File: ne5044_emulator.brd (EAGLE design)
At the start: 17 x 23 mm, 13 parts, among them IC2 STM8S003F3, U1 NE5044_MINIMAL_PADS, U2 SPX1117M3-L-5-0

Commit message: - Daily save
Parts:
- moved SWIM 0.51 mm to (2.29, 6.35)
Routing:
- net GND: track 74.9 -> 75.9 mm, vias 4 -> 3
- net BTN0: track 35.4 -> 34.5 mm
- net BTN1: track 15.2 -> 14.3 mm
- net ADC_CH0: track 9.11 -> 9.95 mm
- net +5V: track 34.5 -> 33.7 mm
- net BTN2: track 16.0 -> 15.3 mm
- net ADC_CH2: track 10.5 -> 9.90 mm
- net BTN3: track 16.9 -> 16.3 mm
- net !STM8_RESET: track 14.1 -> 13.6 mm
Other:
- board size 17 x 23 mm -> 16.5 x 23 mm
- board text added: "BTN0"
- board text added: "BTN1"
- board text added: "BTN2"
- board text added: "BTN3"
- board text added: "CAL"

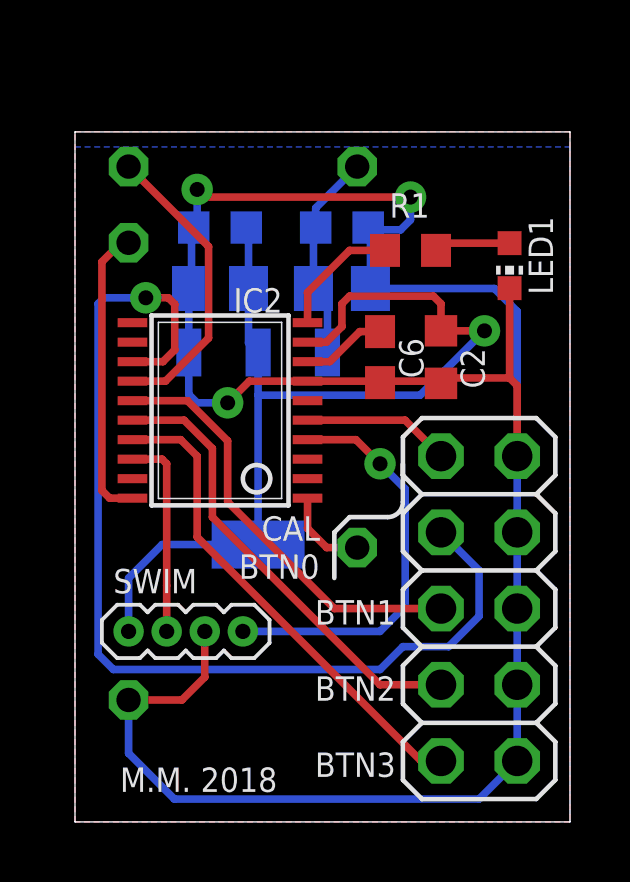
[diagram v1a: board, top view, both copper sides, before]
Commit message: - Add output transistor
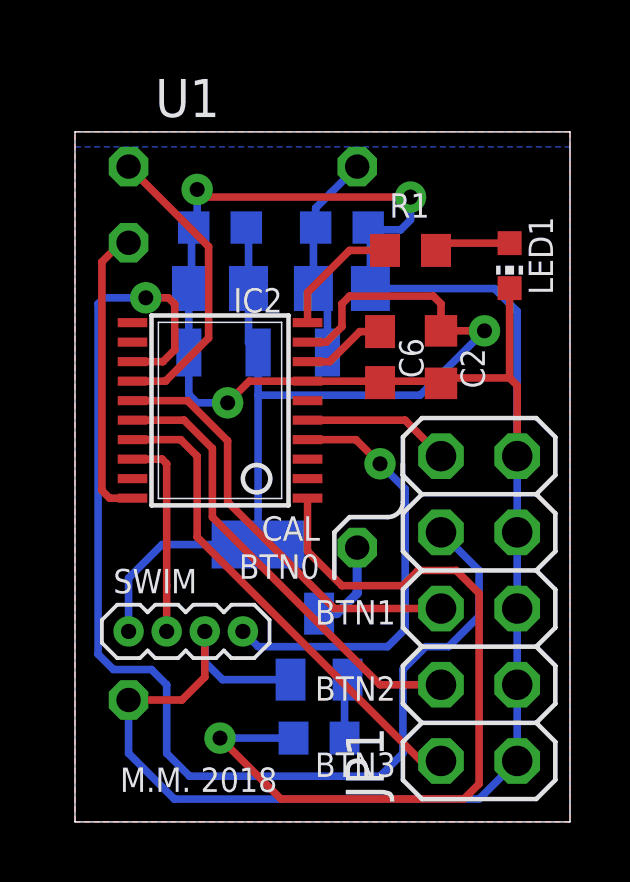
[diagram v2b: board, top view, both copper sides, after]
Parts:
- added Q1: BC847ALT1SMD, transistor-npn:SOT23
- added R2: 1K, rcl:R0603
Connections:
- new net ENCODED_SIGNAL_OC: Q1.3, U1.11
- new net N$2: Q1.1, R2.1
- net ENCODED_SIGNAL: now also R2.2; no longer U1.11
- net GND: now also Q1.2
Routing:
- net ENCODED_SIGNAL: track 2.93 -> 27.0 mm, vias 0 -> 1
- net BTN0: track 34.5 -> 40.4 mm
- net GND: track 75.9 -> 80.0 mm
- net ENCODED_SIGNAL_OC: track 0.00 -> 3.07 mm
- net N$2: track 0.00 -> 1.99 mm
- net !STM8_RESET: track 13.6 -> 14.5 mm
